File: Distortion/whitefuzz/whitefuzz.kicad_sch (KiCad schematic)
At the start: 27 parts, among them J1 Conn_01x04_Female, Q2 2n5088, Q3 2n5457

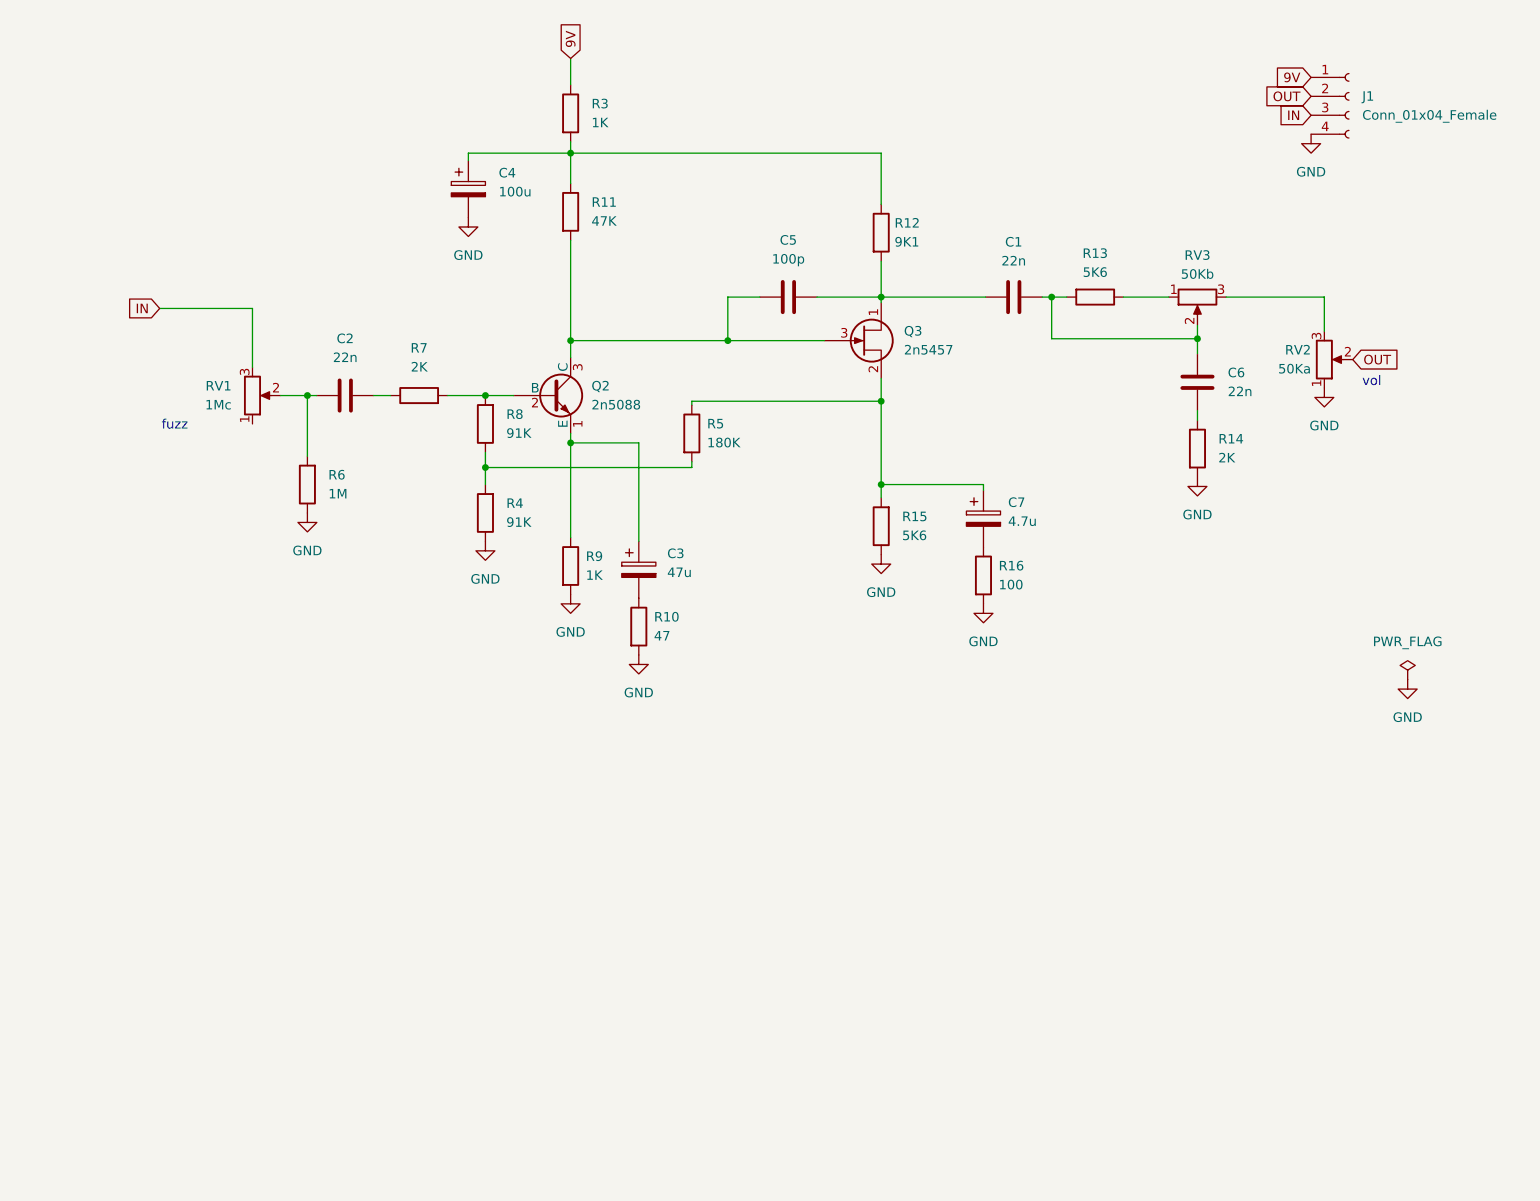
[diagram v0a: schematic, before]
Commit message: replaced whiefuzz, and modified ejfuzzface
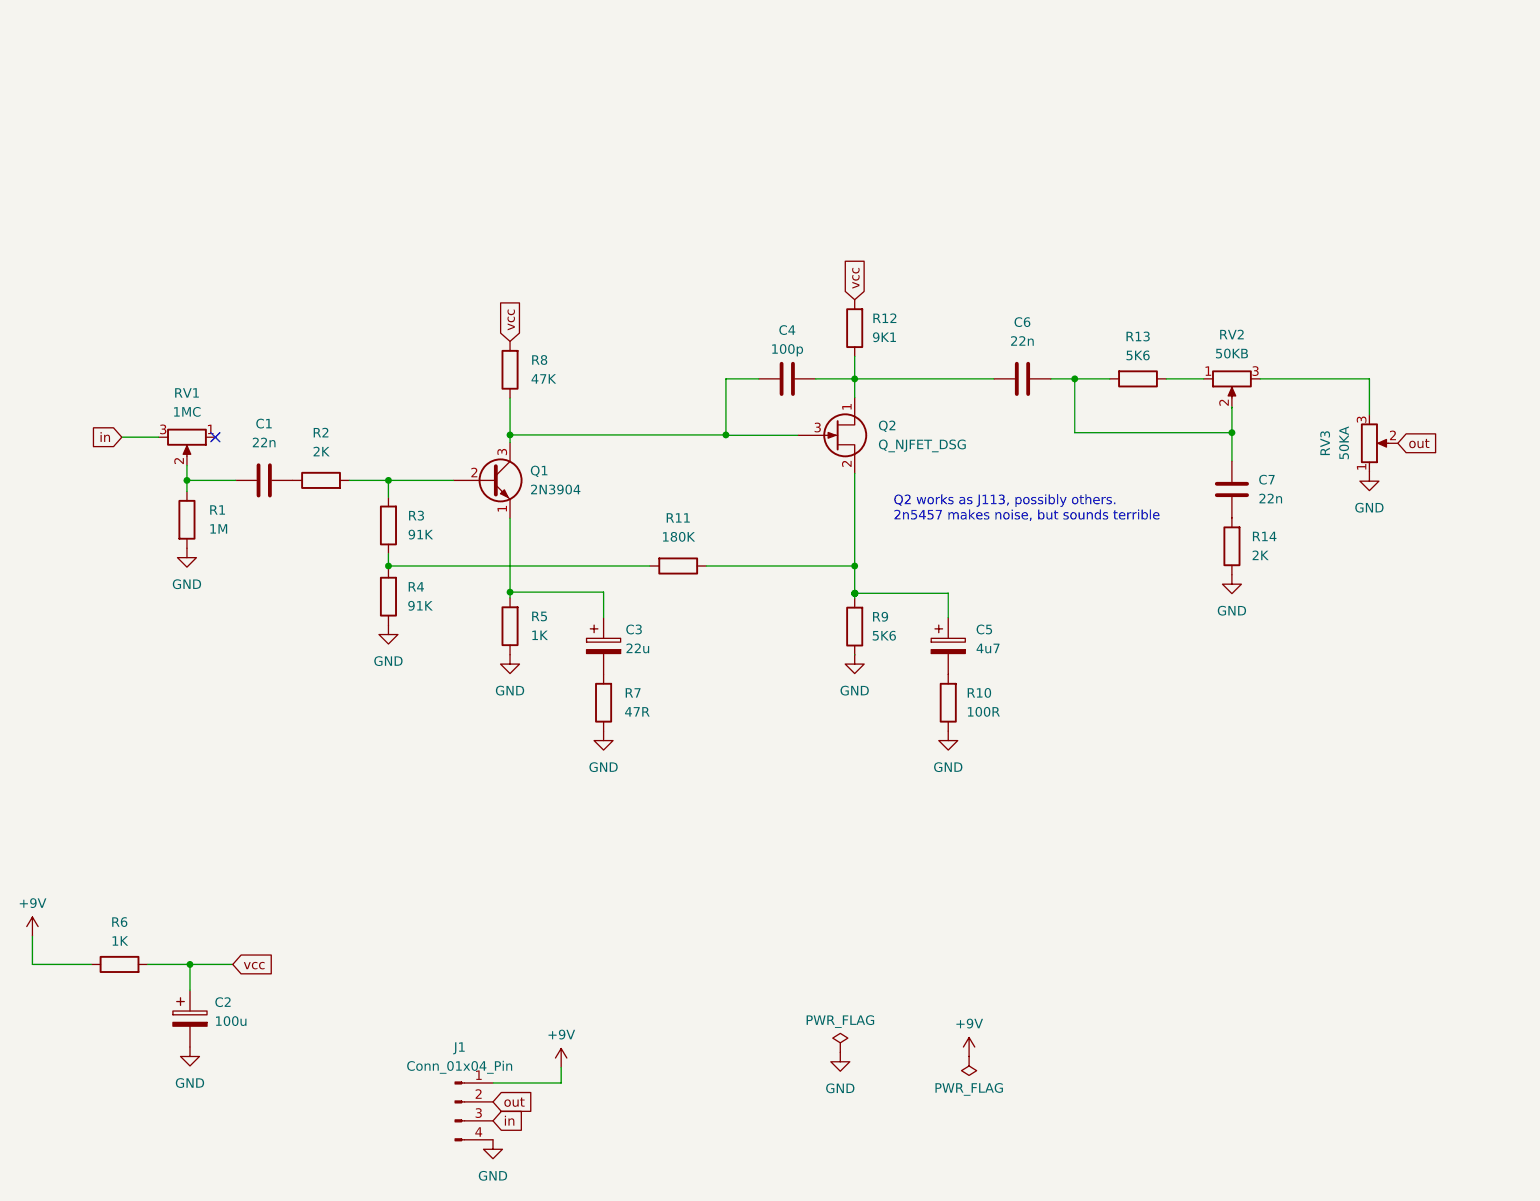
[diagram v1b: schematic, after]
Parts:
- removed C2: 22n, Capacitor_THT:C_Disc_D7.5mm_W2.5mm_P5.00mm, symbol Device:C
- removed C4: 100u, Capacitor_THT:CP_Radial_D6.3mm_P2.50mm, symbol Device:C_Polarized
- removed C5: 100p, Capacitor_THT:C_Disc_D7.5mm_W2.5mm_P5.00mm, symbol Device:C
- removed C7: 4.7u, Capacitor_THT:CP_Radial_D5.0mm_P2.00mm, symbol Device:C_Polarized
- removed J1: Conn_01x04_Female, Connector_PinHeader_2.54mm:PinHeader_1x04_P2.54mm_Vertical, symbol Connector:Conn_01x04_Female
- removed Q2: 2n5088, Package_TO_SOT_THT:TO-92_Inline, symbol Transistor_BJT:2N3904
- removed Q3: 2n5457, Package_TO_SOT_THT:TO-92_Inline, symbol Device:Q_NJFET_DSG
- removed R15: 5K6, Resistor_THT:R_Axial_DIN0207_L6.3mm_D2.5mm_P7.62mm_Horizontal, symbol Device:R
- removed R16: 100, Resistor_THT:R_Axial_DIN0207_L6.3mm_D2.5mm_P7.62mm_Horizontal, symbol Device:R
- added C2: 100u, Capacitor_THT:CP_Radial_D6.3mm_P2.50mm, symbol Device:C_Polarized
- added C4: 100p, Capacitor_THT:C_Disc_D5.0mm_W2.5mm_P2.50mm, symbol Device:C
- added C5: 4u7, Capacitor_THT:CP_Radial_D5.0mm_P2.00mm, symbol Device:C_Polarized
- added C7: 22n, Capacitor_THT:C_Rect_L7.0mm_W2.5mm_P5.00mm, symbol Device:C
- added J1: Conn_01x04_Pin, Connector_PinHeader_2.54mm:PinHeader_1x04_P2.54mm_Vertical, symbol Connector:Conn_01x04_Pin
- added Q1: 2N3904, Package_TO_SOT_THT:TO-92_Inline, symbol Transistor_BJT:2N3904
- added Q2: Q_NJFET_DSG, Package_TO_SOT_THT:TO-92, symbol Device:Q_NJFET_DSG
- added R1: 1M, Resistor_THT:R_Axial_DIN0207_L6.3mm_D2.5mm_P10.16mm_Horizontal, symbol Device:R
- added R2: 2K, Resistor_THT:R_Axial_DIN0207_L6.3mm_D2.5mm_P10.16mm_Horizontal, symbol Device:R
- C1, C6: footprint Capacitor_THT:C_Disc_D7.5mm_W2.5mm_P5.00mm -> Capacitor_THT:C_Rect_L7.0mm_W2.5mm_P5.00mm
- C3: value 47u -> 22u
- R10: value 47 -> 100R; footprint Resistor_THT:R_Axial_DIN0207_L6.3mm_D2.5mm_P7.62mm_Horizontal -> Resistor_THT:R_Axial_DIN0207_L6.3mm_D2.5mm_P10.16mm_Horizontal
- R11: value 47K -> 180K; footprint Resistor_THT:R_Axial_DIN0207_L6.3mm_D2.5mm_P7.62mm_Horizontal -> Resistor_THT:R_Axial_DIN0207_L6.3mm_D2.5mm_P10.16mm_Horizontal
- R12, R13, R14, R4: footprint Resistor_THT:R_Axial_DIN0207_L6.3mm_D2.5mm_P7.62mm_Horizontal -> Resistor_THT:R_Axial_DIN0207_L6.3mm_D2.5mm_P10.16mm_Horizontal
- R3: value 1K -> 91K; footprint Resistor_THT:R_Axial_DIN0207_L6.3mm_D2.5mm_P7.62mm_Horizontal -> Resistor_THT:R_Axial_DIN0207_L6.3mm_D2.5mm_P10.16mm_Horizontal
- R5: value 180K -> 1K; footprint Resistor_THT:R_Axial_DIN0207_L6.3mm_D2.5mm_P7.62mm_Horizontal -> Resistor_THT:R_Axial_DIN0207_L6.3mm_D2.5mm_P10.16mm_Horizontal
- R6: value 1M -> 1K; footprint Resistor_THT:R_Axial_DIN0207_L6.3mm_D2.5mm_P7.62mm_Horizontal -> Resistor_THT:R_Axial_DIN0207_L6.3mm_D2.5mm_P10.16mm_Horizontal
- R7: value 2K -> 47R; footprint Resistor_THT:R_Axial_DIN0207_L6.3mm_D2.5mm_P7.62mm_Horizontal -> Resistor_THT:R_Axial_DIN0207_L6.3mm_D2.5mm_P10.16mm_Horizontal
- R8: value 91K -> 47K; footprint Resistor_THT:R_Axial_DIN0207_L6.3mm_D2.5mm_P7.62mm_Horizontal -> Resistor_THT:R_Axial_DIN0207_L6.3mm_D2.5mm_P10.16mm_Horizontal
- R9: value 1K -> 5K6; footprint Resistor_THT:R_Axial_DIN0207_L6.3mm_D2.5mm_P7.62mm_Horizontal -> Resistor_THT:R_Axial_DIN0207_L6.3mm_D2.5mm_P10.16mm_Horizontal
- RV1: value 1Mc -> 1MC
- RV2: value 50Ka -> 50KB
- RV3: value 50Kb -> 50KA
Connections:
- net 9V is gone; now on an unnamed net: R3.1
- net OUT is gone; now on an unnamed net: RV2.2
- net GND: now also R10.1, R14.1, R5.1, R7.1, R9.1, RV3.1, C2.2, J1.4 (Pin_4), R1.2; no longer R10.2, R14.2, R6.1, R9.2, RV2.1
- net at C3.1: now also R5.2, Q1.1 (E); no longer R9.1
- net at R7.2: now also C3.2; no longer R8.2
- net at R11.2: now also R4.2
- net at C6.1: now also R12.1, C4.2, Q2.1 (D); no longer R14.1
- net at C6.2, R13.2: now also C7.2; no longer C1.1, RV3.2
- net at C1.2: now also R2.1; no longer R12.2
- net at RV1.2: now also C1.1, R1.1; no longer R6.2
- net at R13.1: now also RV2.1; no longer RV3.1
- net IN renamed in
- net in: now also J1.3 (Pin_3)
- new net: C5.1, Q2.2 (S), R11.1, R9.2
- new net: C5.2, R10.2
- new net: C4.1, Q1.3 (C), Q2.3 (G), R8.1
- new net: Q1.2 (B), R2.2, R3.2
- new net: C7.1, R14.2
- new net +9V: J1.1 (Pin_1), R6.1
- new net out: J1.2 (Pin_2), RV3.2
- new net vcc: C2.1, R12.2, R6.2, R8.2
- no-connect marks 0 -> 1
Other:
- note added: "Q2 works as J113, possibly others. 2n5457 makes noise, but sounds terrible"
- note removed: "fuzz"
- note removed: "vol"
